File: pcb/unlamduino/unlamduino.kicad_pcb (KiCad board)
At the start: 2 copper layers, 41 parts, among them IC2 ATMEGA328-P, P3 CONN_01X08, U1 LM2576, U2 AP111733, Y2 16MHz

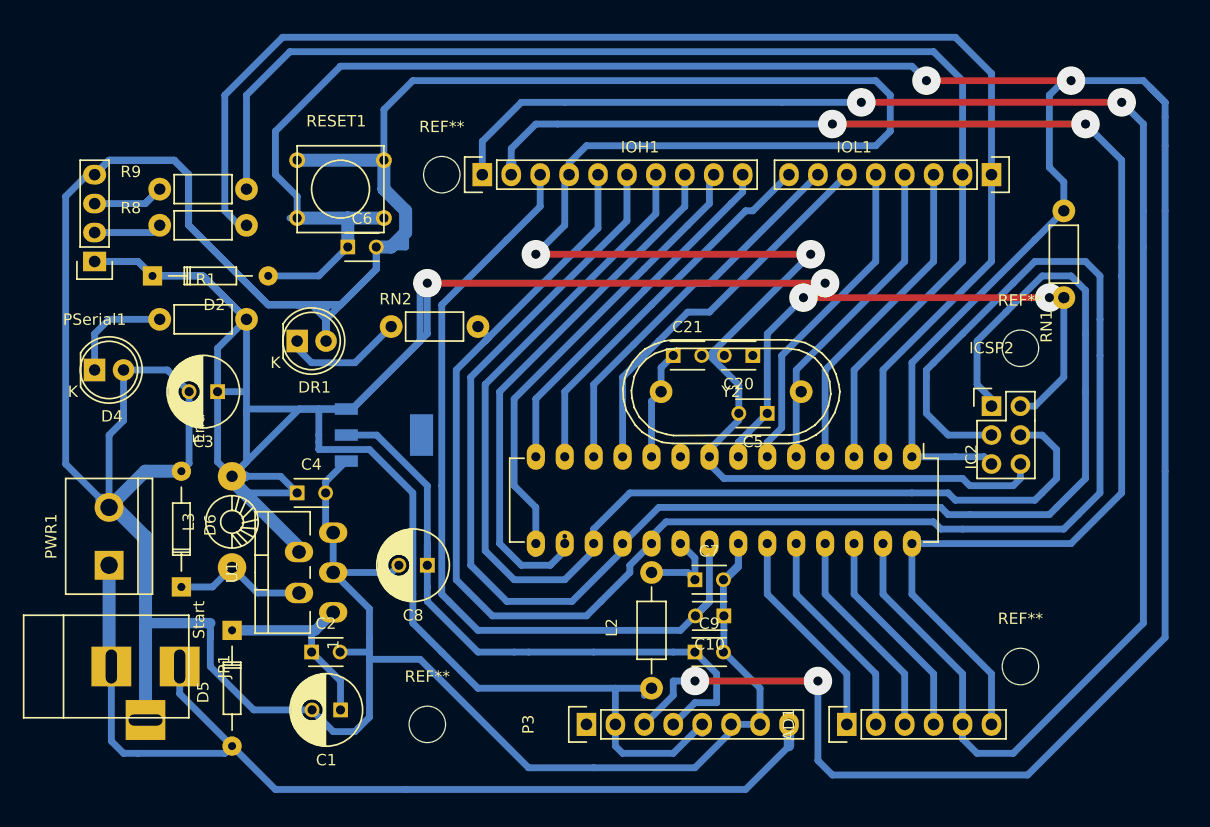
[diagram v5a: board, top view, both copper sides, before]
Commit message: Re-acomodo de la fuente y consolidacion de 8 puentes. Relleno de zonas.
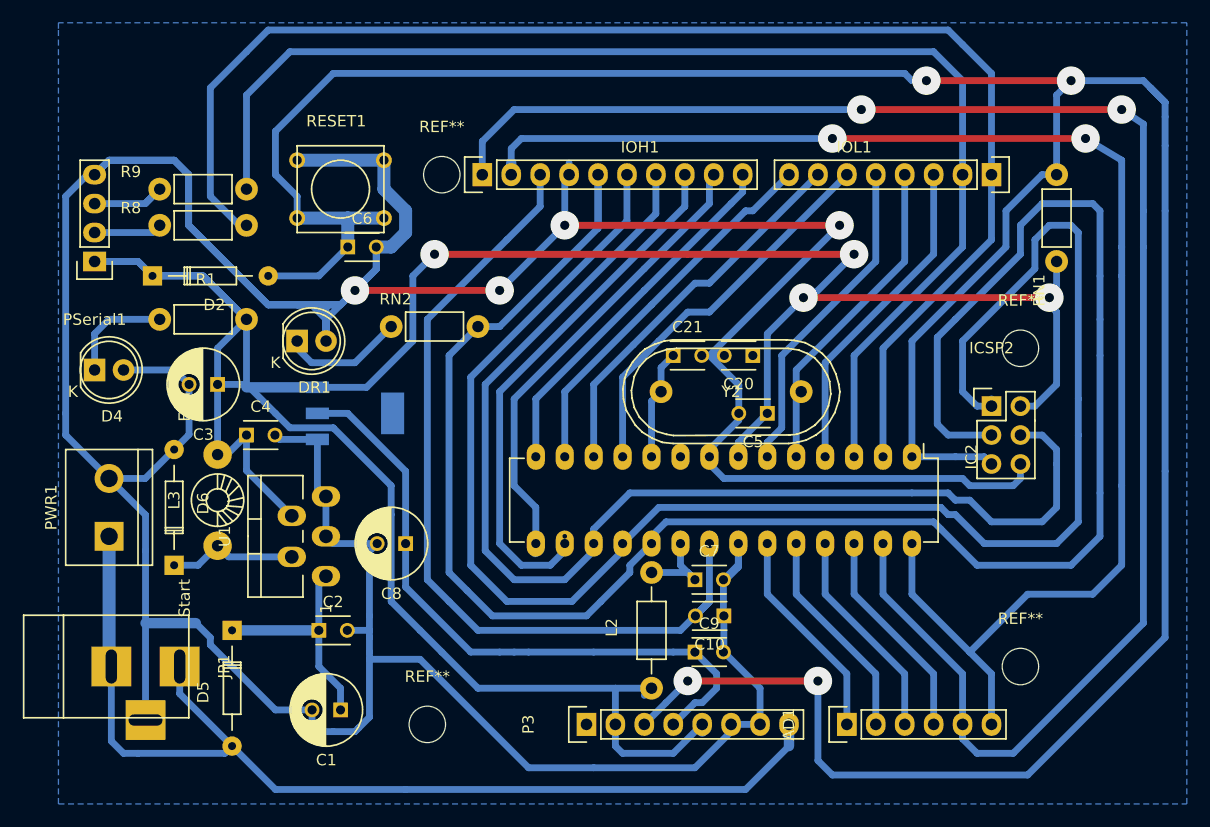
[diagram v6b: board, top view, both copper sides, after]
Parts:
- moved C4 6.75 mm to (175.3, 75.6)
- moved RN1 3.24 mm to (246.4, 60.3)
- moved U1 3.24 mm to (178.4, 84.5)
- moved U2 3.17 mm to (184.8, 73.7)
- moved C8 2.69 mm to (189.2, 85.1)
- moved PWR1 2.54 mm to (163.2, 81.9)
- moved L3 2.29 mm to (172.7, 81.3)
- moved C2 2.01 mm to (181.6, 92.7)
- moved D6 2.01 mm to (168.9, 87.0)
- moved C3 0.63 mm to (172.7, 71.1)
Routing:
- net GND: track 526.4 -> 423.7 mm, vias 2 -> 4
- net +5V: track 297.5 -> 255.6 mm
- net /IO13: track 155.8 -> 174.6 mm
- net /IO12: track 135.8 -> 150.2 mm
- net /IO11: track 102.0 -> 105.1 mm
- net /IO0: track 120.9 -> 123.6 mm
- net /RESET: track 266.5 -> 263.9 mm
- net /VIN: track 91.6 -> 94.1 mm
- net Net-(C1-Pad1): track 22.2 -> 20.1 mm
- net /AD5/SCL: track 128.6 -> 129.9 mm
- net /AREF: track 74.9 -> 75.9 mm
- net Net-(D6-Pad1): track 13.5 -> 12.5 mm
- net +3V3: track 56.2 -> 56.9 mm
- net /AD4/SDA: track 148.2 -> 147.5 mm
- added copper zone on B.Cu, net GND

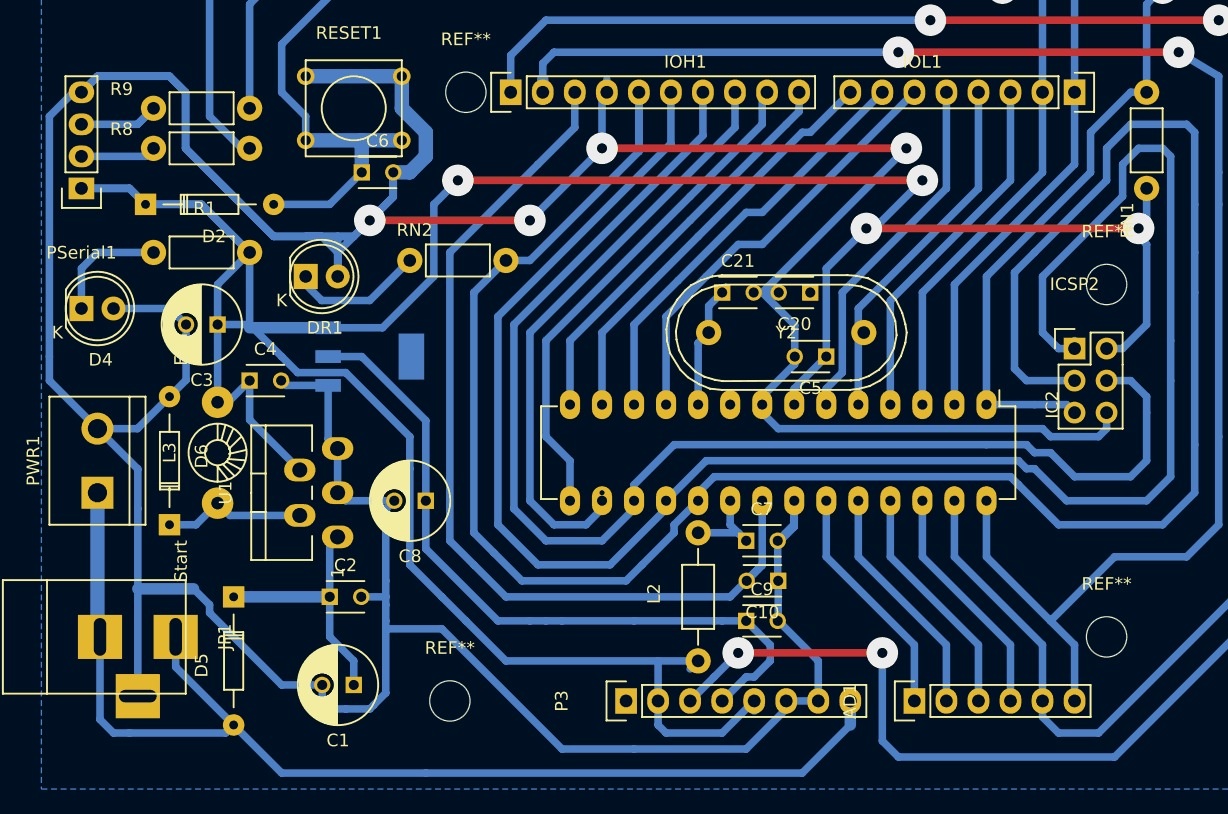
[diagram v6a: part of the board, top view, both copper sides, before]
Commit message: Cambio de ancho en algunas pistas.
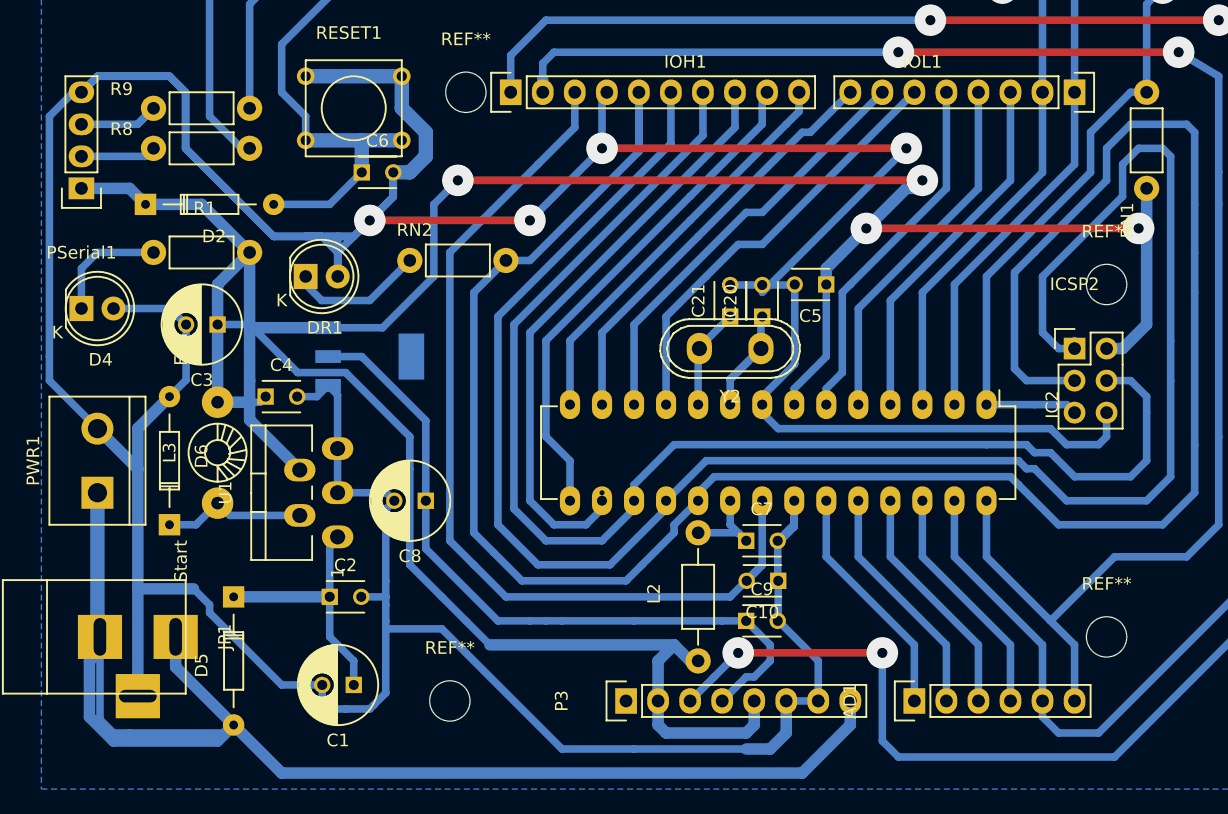
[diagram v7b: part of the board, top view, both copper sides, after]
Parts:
- Y2: footprint Crystals:Crystal_HC51-U_Vertical -> Crystals:Crystal_HC50-U_Vertical
- moved C5 5.72 mm to (221.0, 67.9)
- moved Y2 4.62 mm to (213.4, 73.0)
- moved C20 4.26 mm to (215.9, 70.5), turned to 90 degrees
- moved C21 2.01 mm to (213.4, 70.5), turned to 90 degrees
- moved C4 1.80 mm to (176.5, 76.8)
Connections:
- P3 pad 1: Net-(P3-Pad1) -> (no net)
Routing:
- net /VIN: track 94.1 -> 166.7 mm
- net +5V: track 255.6 -> 315.1 mm
- net GND: track 423.7 -> 447.3 mm
- net /XTAL1: track 0.00 -> 11.5 mm
- net /XTAL2: track 9.68 -> 8.43 mm

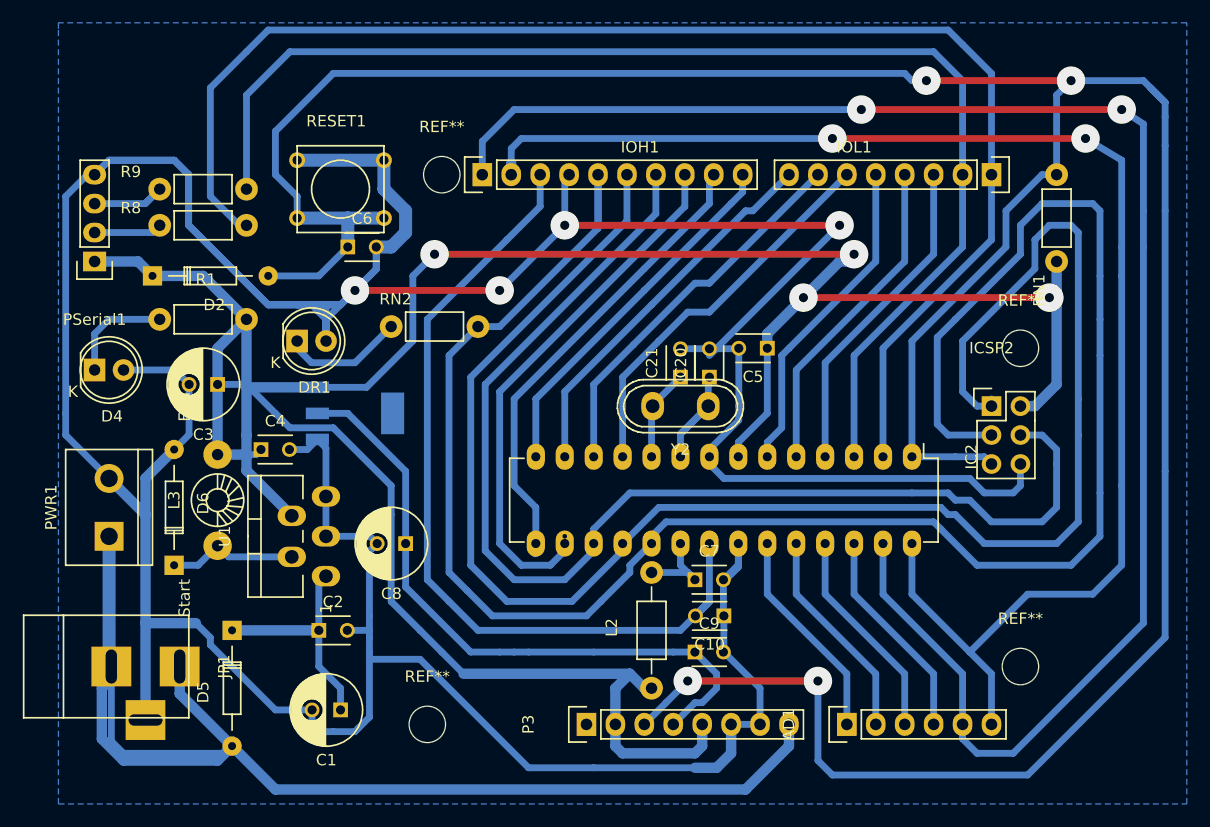
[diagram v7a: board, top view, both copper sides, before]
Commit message: Pistas gruesas en fuente, cambio de agujeros de fijación a los que dice el sch
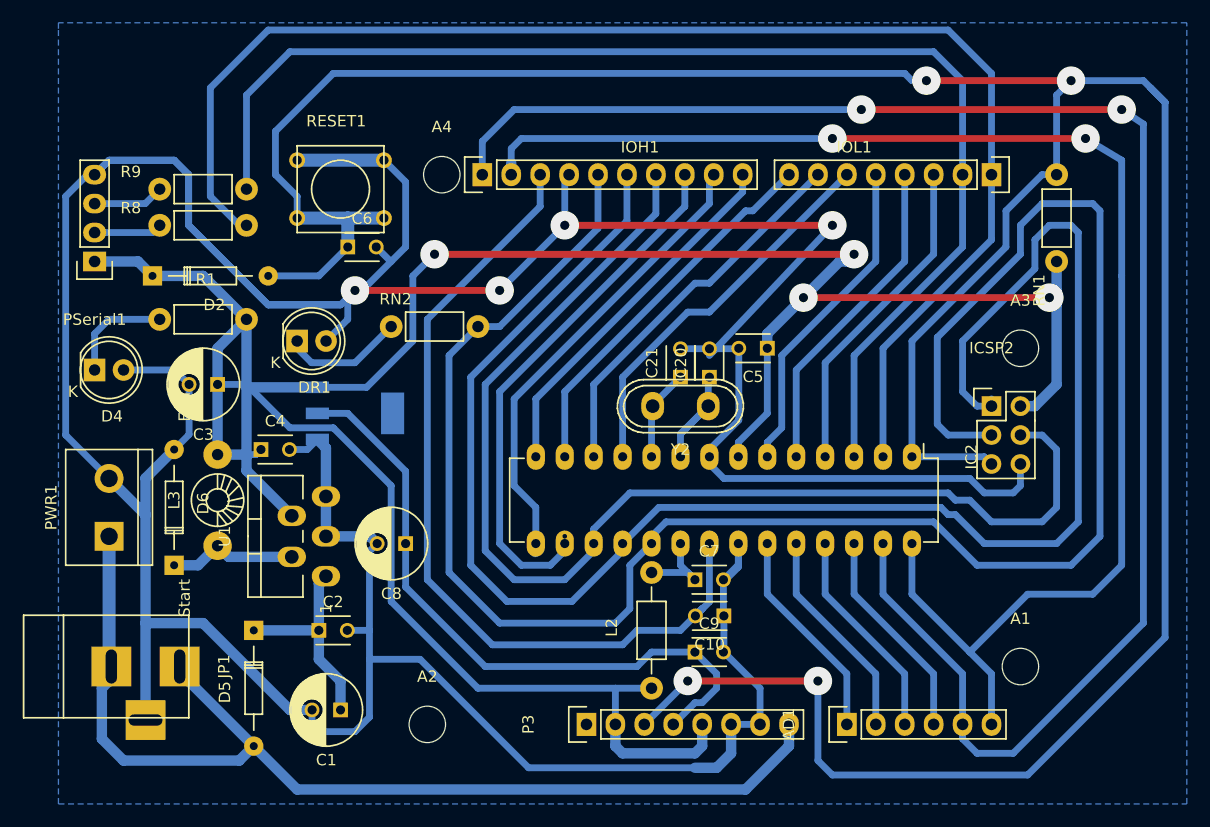
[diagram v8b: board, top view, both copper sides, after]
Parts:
- removed REF** (x4): MountingHole_3.2mm_M3, Mounting_Holes:MountingHole_3.2mm_M3
- added A1: Agujero, Mounting_Holes:MountingHole_3.2mm_M3, F.Cu at (243.2, 95.9)
- added A2: Agujero, Mounting_Holes:MountingHole_3.2mm_M3, F.Cu at (191.1, 101.0)
- added A3: Agujero, Mounting_Holes:MountingHole_3.2mm_M3, F.Cu at (243.2, 67.9)
- added A4: Agujero, Mounting_Holes:MountingHole_3.2mm_M3, F.Cu at (192.4, 52.7)
- moved D5 1.91 mm to (175.9, 92.7)
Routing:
- net /VIN: track 166.7 -> 101.9 mm
- net GND: track 447.3 -> 430.0 mm
- net Net-(D6-Pad1): track 12.5 -> 16.3 mm
- net /IO13: track 174.6 -> 172.3 mm
- net Net-(PSerial1-Pad3): track 8.04 -> 6.24 mm
- net +5V: track 315.1 -> 313.4 mm
- net /AD5/SCL: track 129.9 -> 128.6 mm
- net +3V3: track 56.9 -> 57.9 mm
- net Net-(C1-Pad1): track 20.1 -> 19.1 mm
- net /AREF: track 75.9 -> 75.3 mm
